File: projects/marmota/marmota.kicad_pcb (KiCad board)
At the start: 2 copper layers, 70 x 70 mm, 63 parts, among them J1 USB_C, J2 Conn_01x20_Pin, J3 Conn_01x20_Pin, SW1 Button top, SW2 Button side, U1 RP2040, U2 FLASH, U3 MCP73871, U4 RT6160, U5 ESP32, Y1 12MHz

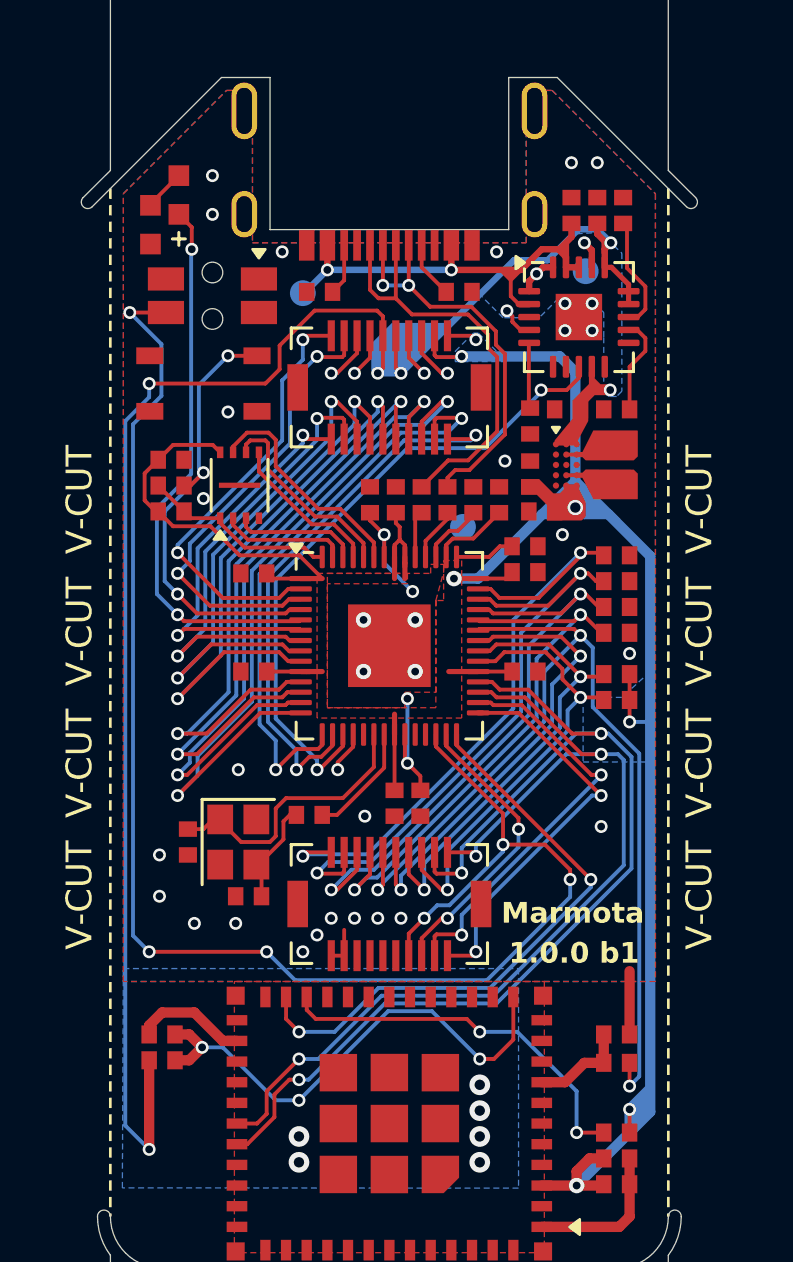
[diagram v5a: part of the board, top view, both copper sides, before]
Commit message: Extra GPIO exposed to connector, Ground plane tweaks
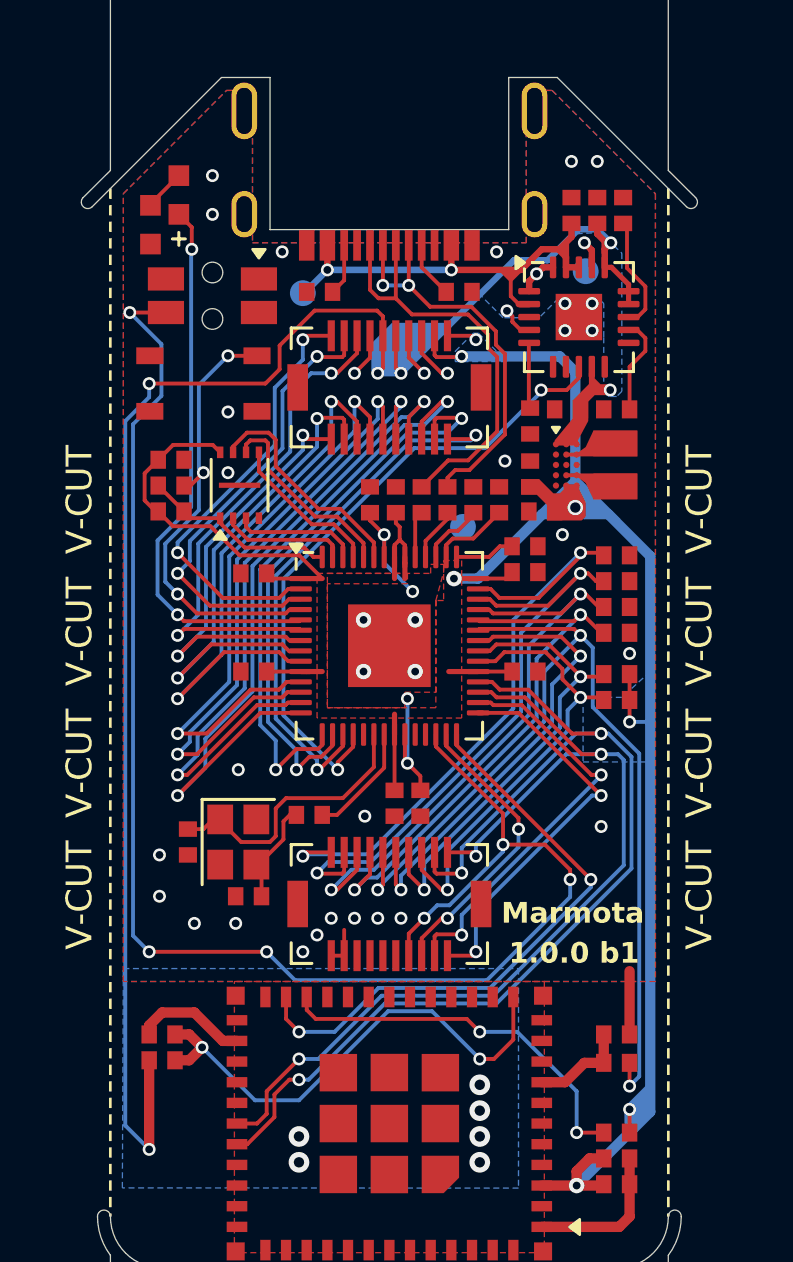
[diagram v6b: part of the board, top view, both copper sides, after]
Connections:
- J2 pad 11: /GP4 -> /GP5
- J2 pad 12: /GP5 -> /GP6
- J2 pad 13: /GP6 -> /GP7
- J2 pad 14: /GP7 -> /GP8
- J2 pad 15: /GP8 -> /GP9
- J2 pad 16: /GP9 -> /GP10
- J2 pad 17: /GP10 -> /GP11
- J2 pad 18: /GP11 -> /GP12
- J2 pad 19: /GP12 -> /GP13
- J2 pad 20: /GP13 -> /GP14
- J2 pad 3: unconnected-(J2-Pin_3-Pad3) -> /GP4
- J2 pad 4: unconnected-(J2-Pin_4-Pad4) -> GND
- U3 pad 8: /GP14 -> /GP15
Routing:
- net /GP15: track 1.61 -> 25.0 mm, vias 1 -> 2
- net /GP4: track 15.8 -> 20.0 mm
- net /GP14: track 25.3 -> 21.2 mm
- net unconnected-(J2-Pin_3-Pad3): track 2.00 -> 0.00 mm, vias 1 -> 0
- net unconnected-(J2-Pin_4-Pad4): track 1.70 -> 0.00 mm, vias 1 -> 0
- net GND: track 13.7 -> 15.4 mm, vias 40 -> 41
- net /GP5: track 18.4 -> 16.9 mm
- net /GP11: track 28.3 -> 27.2 mm
- net /GP6: track 20.6 -> 19.5 mm
- net /GP10: track 26.4 -> 25.6 mm
- net /GP9: track 24.7 -> 24.1 mm
- net /EADC0: vias 3 -> 2

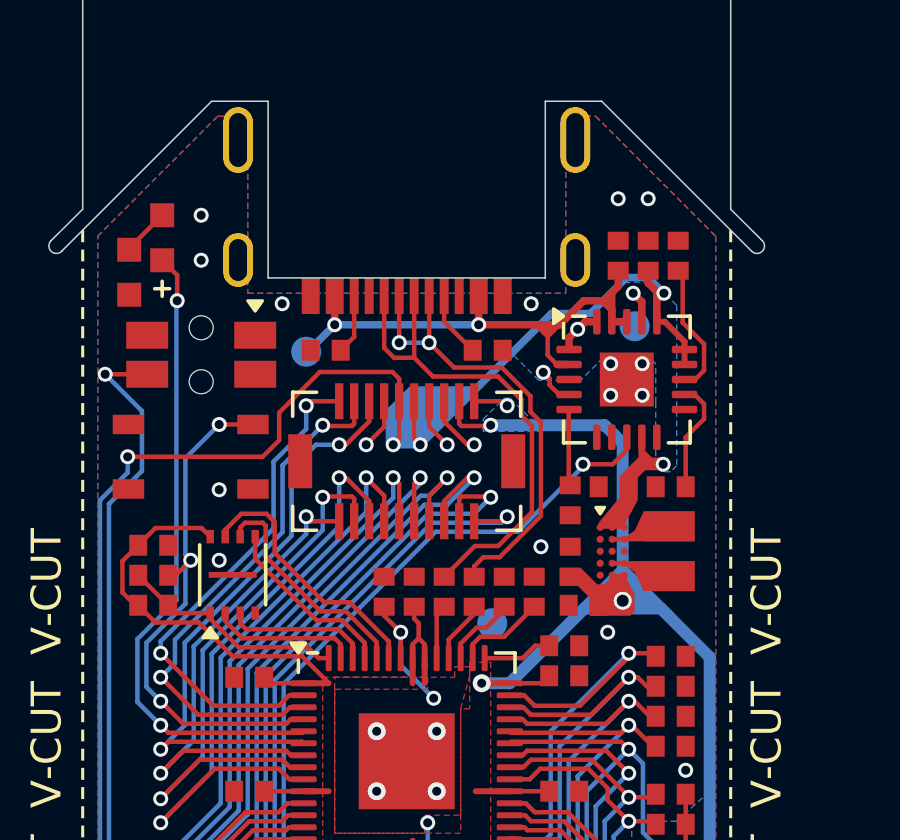
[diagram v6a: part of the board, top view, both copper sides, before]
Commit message: Changed power output caps to 47uF in 0603 footprint
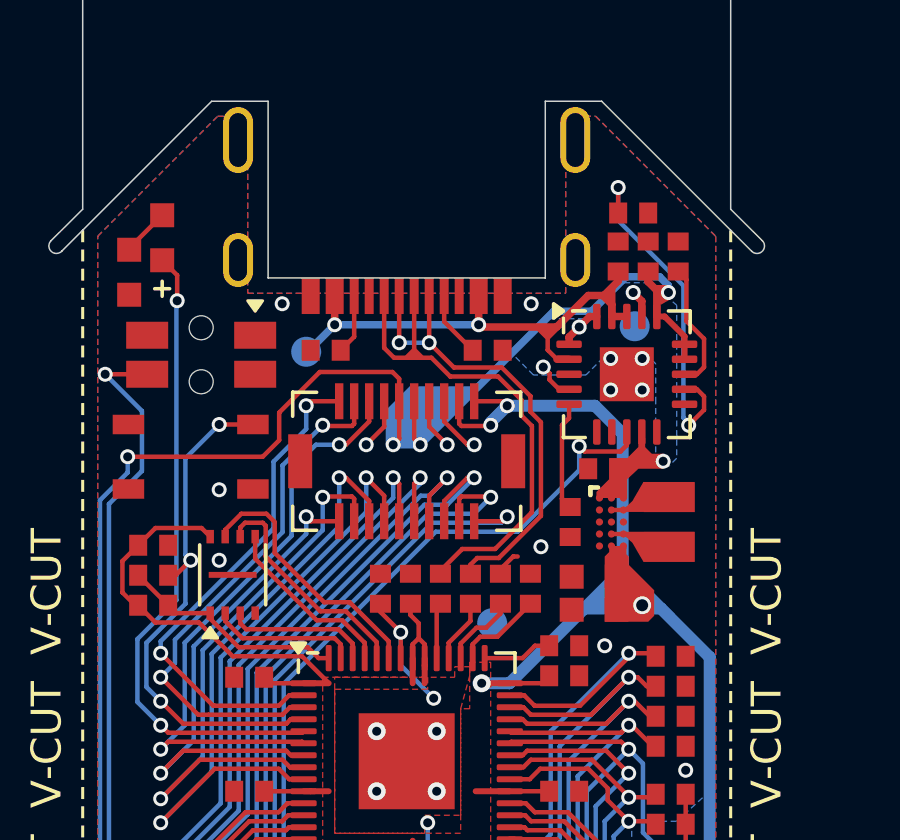
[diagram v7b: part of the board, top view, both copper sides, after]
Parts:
- C42, C43: value 22uF -> 47uF; footprint ILO_fp:0402_compact -> ILO_fp:0603_compact
- moved R33 9.21 mm to (67.5, 33.7), turned to 0 degrees
- moved U4 0.98 mm to (66.8, 44.0)
- moved L1 0.98 mm to (68.8, 44.0)
- moved C42 0.94 mm to (66.2, 45.9), turned to 0 degrees
- moved R34 0.73 mm to (65.5, 44.0)
- moved C41 0.69 mm to (66.5, 42.2)
- moved C43 0.38 mm to (66.2, 47.0)
- moved U3 0.17 mm to (67.3, 39.1)
- moved C10 0.16 mm to (64.1, 46.2)
- moved C6 0.16 mm to (59.1, 46.2)
- moved C8 0.16 mm to (63.1, 46.2)
- moved C9 0.16 mm to (60.1, 46.2)
- moved R3 0.16 mm to (61.1, 46.2)
- moved R4 0.16 mm to (62.1, 46.2)
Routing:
- net Net-(U3-PROG3): track 3.79 -> 11.6 mm, vias 0 -> 2
- net Net-(U3-THERM): track 2.55 -> 3.64 mm
- net +3V3: track 89.8 -> 90.6 mm
- net GND: track 15.4 -> 16.1 mm, vias 41 -> 37
- net /GP15: track 25.0 -> 25.6 mm

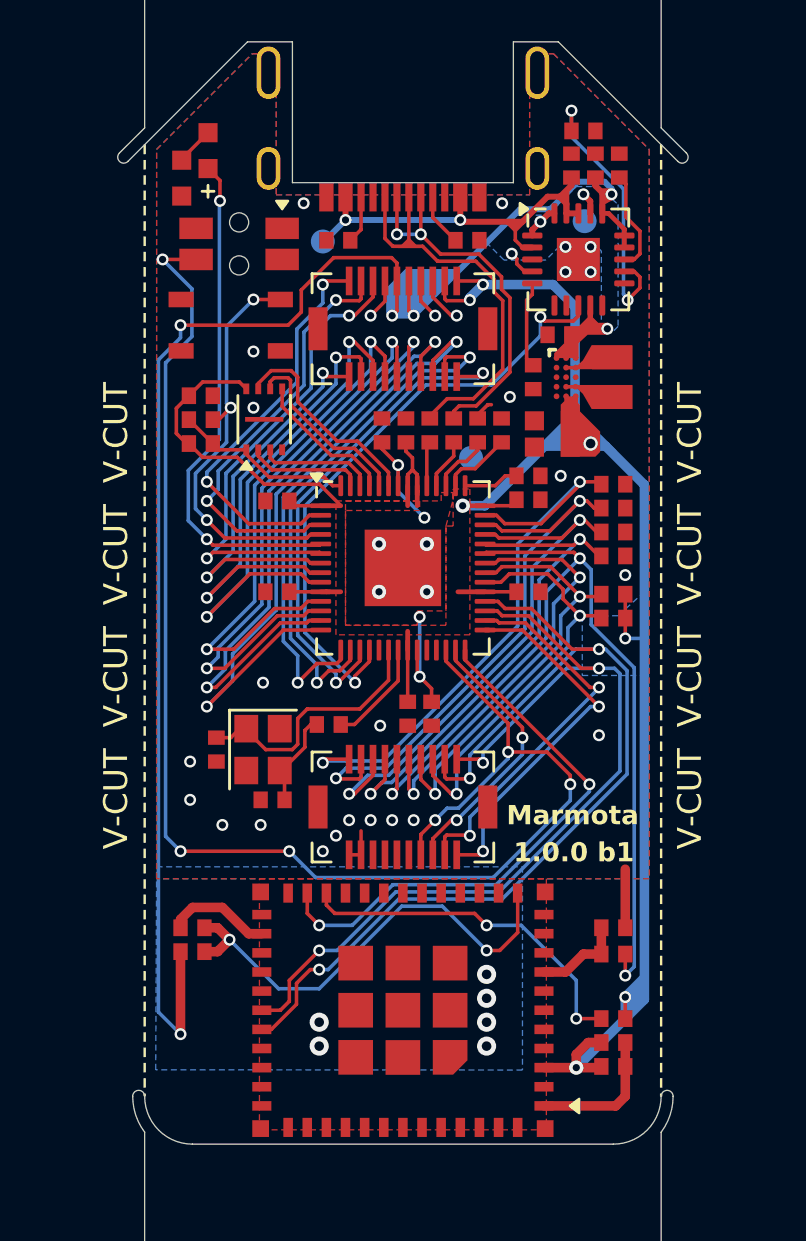
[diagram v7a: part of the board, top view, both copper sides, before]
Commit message: Using Richtek 6150 instead of 6160
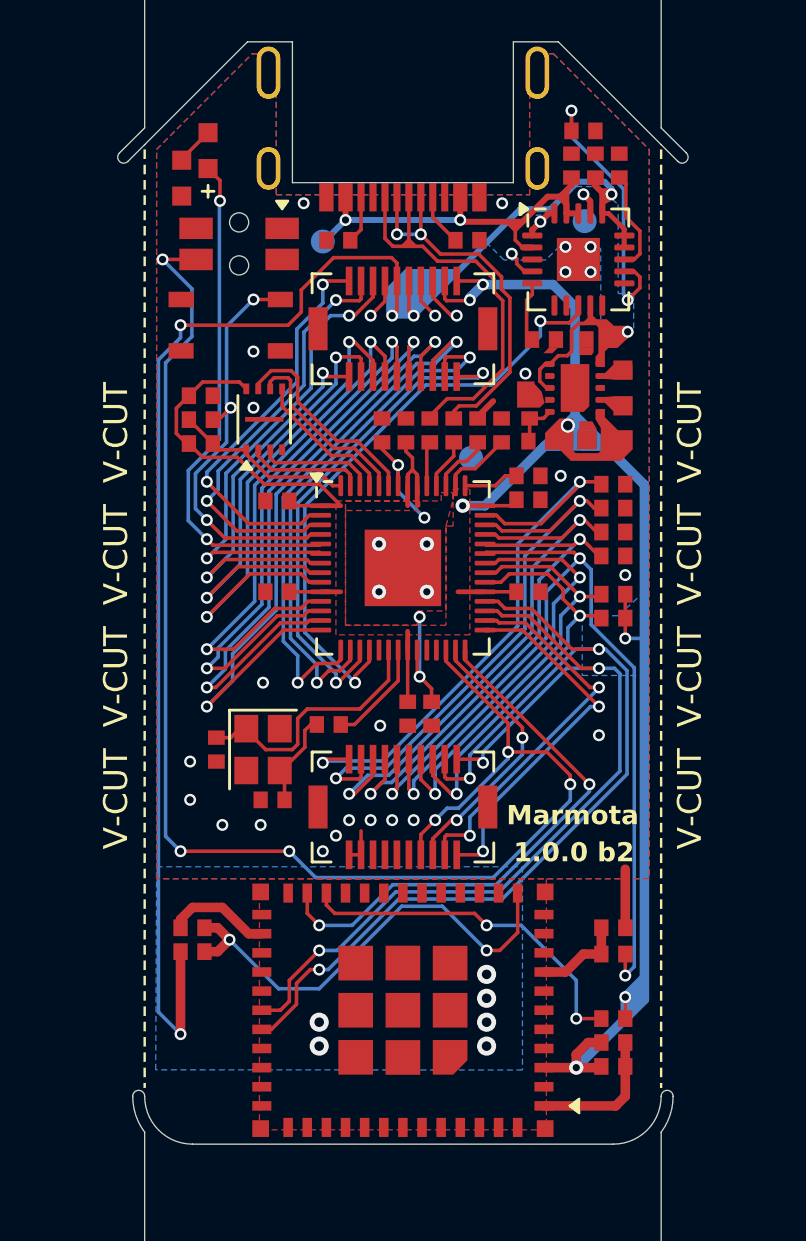
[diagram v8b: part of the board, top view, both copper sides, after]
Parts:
- removed C43: 47uF, ILO_fp:0603_compact
- added R35: 487KΩ, ILO_fp:0402_compact, F.Cu at (65.8, 46.7)
- added R36: 86.6KΩ, ILO_fp:0402_compact, F.Cu at (65.3, 45.2)
- L1: value 0.47uH -> 2.2uH; footprint ILO_fp:SMD_16x10 -> ILO_fp:0603_compact
- U4: value RT6160 -> RT6150B; footprint ILO_fp:WL-CSP-15B-1.4x2.3 -> ILO_fp:WDFN-10L-2.5x2.5
- moved C42 2.34 mm to (68.5, 46.6)
- moved R34 1.64 mm to (65.9, 42.5), turned to 0 degrees
- moved C41 1.64 mm to (68.2, 42.5)
- moved L1 0.64 mm to (69.2, 44.5)
- moved U4 0.59 mm to (67.2, 44.5), turned to 90 degrees
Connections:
- L1 pad 1: Net-(L1-Pad1) -> Net-(U4-LX2)
- L1 pad 2: Net-(L1-Pad2) -> Net-(U4-LX1)
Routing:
- net VSYS: track 3.66 -> 8.73 mm
- net Net-(U4-FB): track 0.00 -> 1.93 mm
- net Net-(U3-THERM): track 3.64 -> 2.54 mm
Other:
- board text added: "1.0.0 b2"
- board text added: "Input Labs Oy. Marmota 1.0.0 beta2"
- board text removed: "1.0.0 b1"
- board text removed: "Input Labs Oy. Marmota 1.0.0 beta1"
